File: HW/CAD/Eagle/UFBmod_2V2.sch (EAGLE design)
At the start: 210 parts, among them J1411 ABRACON_ARJE-0034, T0551 MMBT2222, U0501 MIDAS_MCCOG21605B6W-FPTLWI, U0601 MAX5217, U0651 LM4120IM5-3.0, U0701 AT86RF215-ZU, U0711 ASVTX-13-D-26.000MHZ-I05-T, U0811 PE4259, U0821 RFX1010, U0881 B39871B3440U410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

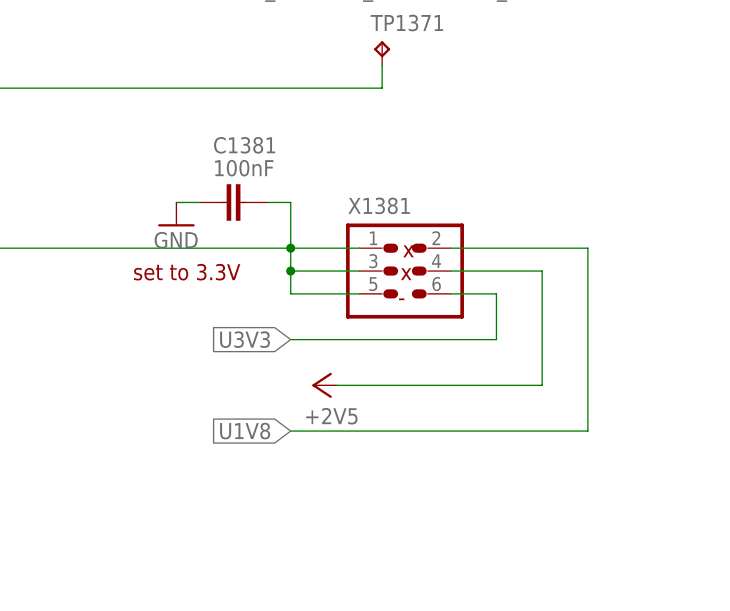
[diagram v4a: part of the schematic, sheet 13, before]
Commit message: HW - EAGLE - V2.2 devices placed
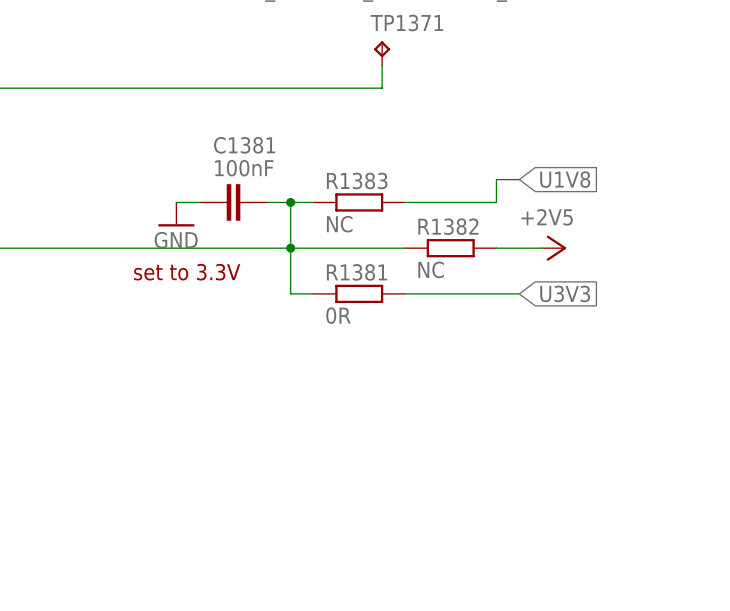
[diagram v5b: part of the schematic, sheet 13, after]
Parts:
- removed R0951, R0952: 0R, df4iah_rcl:R-EU_R0402
- removed X1381: (no value), df4iah_connector:HEADER-2X3
- added R1381: 0R, df4iah_rcl:R-EU_R0402
- added R1382, R1383: NC, df4iah_rcl:R-EU_R0402
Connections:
- removed net N$1: R0951.2, U0911.D_M
- removed net N$3: R0952.2, U0911.D_P
- net +2V5: now also R1382.2; no longer X1381.4
- net U1V8: now also R1383.2; no longer X1381.2
- net U3V3: now also R1381.2; no longer X1381.6
- net USB_D_N: now also U0911.D_M; no longer R0951.1
- net USB_D_P: now also U0911.D_P; no longer R0952.1
- net VCCIO16: now also R1381.1, R1382.1, R1383.1; no longer X1381.1, X1381.3, X1381.5
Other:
- note removed: "-"
- note removed: "x"
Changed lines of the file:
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@@
 <part name="R1365" library="df4iah_rcl" deviceset="R-EU_" device="R0402" value="100R"/>
 <part name="R1366" library="df4iah_rcl" deviceset="R-EU_" device="R0402" value="100R"/>
-<part name="X1381" library="df4iah_connector" deviceset="HEADER-2X3" device=""/>
 <part name="+2V5_1350" library="df4iah_supply" deviceset="+2V5" device=""/>
 <part name="C1381" library="df4iah_rcl" deviceset="C-EU" device="C0402" value="100nF"/>
@@
 <part name="C0917" library="df4iah_rcl" deviceset="C-EU" device="C0402" value="100nF"/>
 <part name="C0918" library="df4iah_rcl" deviceset="C-EU" device="C0402" value="100nF"/>
-<part name="R0951" library="df4iah_rcl" deviceset="R-EU_" device="R0402" value="0R"/>
-<part name="R0952" library="df4iah_rcl" deviceset="R-EU_" device="R0402" value="0R"/>
 <part name="+3V3_0901" library="df4iah_supply" deviceset="+3V3" device=""/>
 <part name="U0651" library="df4iah_powersupply" deviceset="LM4120IM5-3.0" device=""/>
 <part name="GND0651" library="df4iah_supply" deviceset="GND" device=""/>
 <part name="C0651" library="df4iah_rcl" deviceset="C-EU" device="C0402" value="100nF"/>
+<part name="R1381" library="df4iah_rcl" deviceset="R-EU_" device="R0402" value="0R"/>
+<part name="R1382" library="df4iah_rcl" deviceset="R-EU_" device="R0402" value="NC"/>
+<part name="R1383" library="df4iah_rcl" deviceset="R-EU_" device="R0402" value="NC"/>
 </parts>
 <sheets>
@@
 <instance part="C0917" gate="G$1" x="154.94" y="139.7" rot="R90"/>
 <instance part="C0918" gate="G$1" x="144.78" y="137.16" rot="R90"/>
-<instance part="R0951" gate="G$1" x="83.82" y="111.76"/>
-<instance part="R0952" gate="G$1" x="91.44" y="109.22"/>
 <instance part="+3V3_0901" gate="G$1" x="17.78" y="134.62"/>
 </instances>
@@
 <segment>
 <label x="38.1" y="111.76" size="1.778" layer="95" rot="R180" xref="yes"/>
-<pinref part="R0951" gate="G$1" pin="1"/>
-<wire x1="38.1" y1="111.76" x2="78.74" y2="111.76" width="0.1524" layer="91"/>
+<wire x1="38.1" y1="111.76" x2="104.14" y2="111.76" width="0.1524" layer="91"/>
+<pinref part="U0911" gate="G$1" pin="D_M"/>
 </segment>
 </net>
@@
 <segment>
 <label x="38.1" y="109.22" size="1.778" layer="95" rot="R180" xref="yes"/>
-<pinref part="R0952" gate="G$1" pin="1"/>
-<wire x1="38.1" y1="109.22" x2="86.36" y2="109.22" width="0.1524" layer="91"/>
+<wire x1="38.1" y1="109.22" x2="104.14" y2="109.22" width="0.1524" layer="91"/>
+<pinref part="U0911" gate="G$1" pin="D_P"/>
 </segment>
 </net>
@@
 </segment>
 </net>
-<net name="N$2" class="0">
-<segment>
-<junction x="134.62" y="137.16"/>
-</segment>
-</net>
-<net name="N$1" class="0">
-<segment>
-<pinref part="U0911" gate="G$1" pin="D_M"/>
-<pinref part="R0951" gate="G$1" pin="2"/>
-<wire x1="104.14" y1="111.76" x2="88.9" y2="111.76" width="0.1524" layer="91"/>
-</segment>
-</net>
-<net name="N$3" class="0">
-<segment>
-<pinref part="U0911" gate="G$1" pin="D_P"/>
-<pinref part="R0952" gate="G$1" pin="2"/>
-<wire x1="104.14" y1="109.22" x2="96.52" y2="109.22" width="0.1524" layer="91"/>
-</segment>
-</net>
 <net name="+3V3" class="0">
 <segment>
@@
 <pinref part="D0971" gate="G$1" pin="A"/>
 <wire x1="213.36" y1="96.52" x2="210.82" y2="96.52" width="0.1524" layer="91"/>
-<wire x1="213.36" y1="96.52" x2="213.36" y2="93.98" width="0.1524" layer="91"/>
 <junction x="213.36" y="96.52"/>
 <pinref part="D0972" gate="G$1" pin="A"/>
-<wire x1="213.36" y1="93.98" x2="213.36" y2="86.36" width="0.1524" layer="91"/>
+<wire x1="213.36" y1="96.52" x2="213.36" y2="86.36" width="0.1524" layer="91"/>
 <wire x1="213.36" y1="86.36" x2="210.82" y2="86.36" width="0.1524" layer="91"/>
 <pinref part="C0916" gate="G$1" pin="1"/>
@@
 Digilent JTAG HS3</text>
 <text x="193.294" y="54.864" size="1.778" layer="94">set to 3.3V</text>
-<text x="223.266" y="57.404" size="1.778" layer="94">x</text>
-<text x="223.012" y="54.864" size="1.778" layer="94">x</text>
-<text x="222.758" y="52.07" size="1.778" layer="94">-</text>
 <text x="35.56" y="22.86" size="1.778" layer="97" rot="R90">TI SN75240PWR</text>
 <text x="40.64" y="22.86" size="1.778" layer="97" rot="R90">TI SN75240PWR</text>
@@
 <instance part="R1365" gate="G$1" x="228.6" y="127"/>
 <instance part="R1366" gate="G$1" x="236.22" y="129.54"/>
-<instance part="X1381" gate="G$1" x="223.52" y="55.88"/>
-<instance part="+2V5_1350" gate="G$2" x="213.36" y="43.18" rot="R90"/>
+<instance part="+2V5_1350" gate="G$2" x="241.3" y="58.42" rot="R270"/>
 <instance part="C1381" gate="G$1" x="203.2" y="63.5" smashed="yes" rot="R90">
 <attribute name="NAME" x="202.184" y="68.961" size="1.778" layer="95"/>
@@
 </instance>
 <instance part="GND0001" gate="1" x="114.3" y="20.32"/>
+<instance part="R1381" gate="G$1" x="218.44" y="53.34"/>
+<instance part="R1382" gate="G$1" x="228.6" y="58.42"/>
+<instance part="R1383" gate="G$1" x="218.44" y="63.5"/>
 </instances>
 <busses>
@@
 <net name="VCCIO16" class="0">
 <segment>
-<wire x1="218.44" y1="58.42" x2="210.82" y2="58.42" width="0.1524" layer="91"/>
 <label x="177.8" y="58.42" size="1.778" layer="95" rot="R180" xref="yes"/>
-<pinref part="X1381" gate="G$1" pin="1"/>
 <wire x1="210.82" y1="58.42" x2="177.8" y2="58.42" width="0.1524" layer="91"/>
-<wire x1="210.82" y1="58.42" x2="210.82" y2="55.88" width="0.1524" layer="91"/>
 <junction x="210.82" y="58.42"/>
-<pinref part="X1381" gate="G$1" pin="3"/>
-<wire x1="210.82" y1="55.88" x2="218.44" y2="55.88" width="0.1524" layer="91"/>
-<wire x1="210.82" y1="55.88" x2="210.82" y2="53.34" width="0.1524" layer="91"/>
-<junction x="210.82" y="55.88"/>
-<pinref part="X1381" gate="G$1" pin="5"/>
-<wire x1="210.82" y1="53.34" x2="218.44" y2="53.34" width="0.1524" layer="91"/>
+<wire x1="210.82" y1="58.42" x2="210.82" y2="53.34" width="0.1524" layer="91"/>
 <wire x1="210.82" y1="58.42" x2="210.82" y2="63.5" width="0.1524" layer="91"/>
 <pinref part="C1381" gate="G$1" pin="2"/>
 <wire x1="210.82" y1="63.5" x2="208.28" y2="63.5" width="0.1524" layer="91"/>
+<pinref part="R1381" gate="G$1" pin="1"/>
+<wire x1="210.82" y1="53.34" x2="213.36" y2="53.34" width="0.1524" layer="91"/>
+<pinref part="R1383" gate="G$1" pin="1"/>
+<wire x1="210.82" y1="63.5" x2="213.36" y2="63.5" width="0.1524" layer="91"/>
+<junction x="210.82" y="63.5"/>
+<pinref part="R1382" gate="G$1" pin="1"/>
+<wire x1="210.82" y1="58.42" x2="223.52" y2="58.42" width="0.1524" layer="91"/>
 </segment>
 </net>
 <net name="U1V8" class="0">
 <segment>
-<pinref part="X1381" gate="G$1" pin="2"/>
-<wire x1="228.6" y1="58.42" x2="243.84" y2="58.42" width="0.1524" layer="91"/>
-<wire x1="243.84" y1="58.42" x2="243.84" y2="38.1" width="0.1524" layer="91"/>
-<wire x1="243.84" y1="38.1" x2="210.82" y2="38.1" width="0.1524" layer="91"/>
-<label x="210.82" y="38.1" size="1.778" layer="95" rot="R180" xref="yes"/>
+<label x="236.22" y="66.04" size="1.778" layer="95" xref="yes"/>
+<pinref part="R1383" gate="G$1" pin="2"/>
+<wire x1="236.22" y1="66.04" x2="233.68" y2="66.04" width="0.1524" layer="91"/>
+<wire x1="233.68" y1="66.04" x2="233.68" y2="63.5" width="0.1524" layer="91"/>
+<wire x1="233.68" y1="63.5" x2="223.52" y2="63.5" width="0.1524" layer="91"/>
 </segment>
 </net>
 <net name="U3V3" class="0">
 <segment>
-<pinref part="X1381" gate="G$1" pin="6"/>
-<wire x1="228.6" y1="53.34" x2="233.68" y2="53.34" width="0.1524" layer="91"/>
-<wire x1="233.68" y1="53.34" x2="233.68" y2="48.26" width="0.1524" layer="91"/>
-<wire x1="233.68" y1="48.26" x2="210.82" y2="48.26" width="0.1524" layer="91"/>
-<label x="210.82" y="48.26" size="1.778" layer="95" rot="R180" xref="yes"/>
+<label x="236.22" y="53.34" size="1.778" layer="95" xref="yes"/>
+<pinref part="R1381" gate="G$1" pin="2"/>
+<wire x1="236.22" y1="53.34" x2="223.52" y2="53.34" width="0.1524" layer="91"/>
 </segment>
 </net>
 <net name="+2V5" class="0">
 <segment>
-<pinref part="X1381" gate="G$1" pin="4"/>
-<wire x1="228.6" y1="55.88" x2="238.76" y2="55.88" width="0.1524" layer="91"/>
-<wire x1="238.76" y1="55.88" x2="238.76" y2="43.18" width="0.1524" layer="91"/>
-<wire x1="238.76" y1="43.18" x2="215.9" y2="43.18" width="0.1524" layer="91"/>
 <pinref part="+2V5_1350" gate="G$2" pin="+2V5"/>
+<pinref part="R1382" gate="G$1" pin="2"/>
+<wire x1="238.76" y1="58.42" x2="233.68" y2="58.42" width="0.1524" layer="91"/>
 </segment>
 </net>
